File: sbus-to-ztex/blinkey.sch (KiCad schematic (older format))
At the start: 16 parts

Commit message: Commit first go at v1.2
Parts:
- removed D1, D5: RED, LED_SMD:LED_0805_2012Metric, symbol Device:LED_ALT
- removed D2, D6: ORANGE, LED_SMD:LED_0805_2012Metric, symbol Device:LED_ALT
- removed D3, D7: GREEN, LED_SMD:LED_0805_2012Metric, symbol Device:LED_ALT
- removed D4, D8: BLUE, LED_SMD:LED_0805_2012Metric, symbol Device:LED_ALT
- removed R1, R2, R3, R4, R5, R6, R7, R8: 549, Resistor_SMD:R_0603_1608Metric, symbol Device:R
- added J5: Conn_02x06_Odd_Even, Connector_PinSocket_2.54mm:PinSocket_2x06_P2.54mm_Horizontal, symbol Connector_Generic:Conn_02x06_Odd_Even
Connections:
- net GND: now also J5.3 (Pin_3), J5.4 (Pin_4)
- new net +3V3: J5.1 (Pin_1), J5.2 (Pin_2)
- new net PMOD-10: J5.10 (Pin_10)
- new net PMOD-11: J5.11 (Pin_11)
- new net PMOD-12: J5.12 (Pin_12)
- new net PMOD-5: J5.5 (Pin_5)
- new net PMOD-6: J5.6 (Pin_6)
- new net PMOD-7: J5.7 (Pin_7)
- new net PMOD-8: J5.8 (Pin_8)
- new net PMOD-9: J5.9 (Pin_9)

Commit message: fix footprints for SeeedStudio DRC results
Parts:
- J5: footprint Connector_PinSocket_2.54mm:PinSocket_2x06_P2.54mm_Horizontal -> For_SeeedStudio:PinSocket_2x06_P2.54mm_Horizontal_For_SeeedStudio
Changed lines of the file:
@@
 F 0 "J5" H 5650 2167 50  0000 C CNN
 F 1 "Conn_02x06_Odd_Even" H 5650 2076 50  0000 C CNN
-F 2 "Connector_PinSocket_2.54mm:PinSocket_2x06_P2.54mm_Horizontal" H 5600 1750 50  0001 C CNN
+F 2 "For_SeeedStudio:PinSocket_2x06_P2.54mm_Horizontal_For_SeeedStudio" H 5600 1750 50  0001 C CNN
 F 3 "~" H 5600 1750 50  0001 C CNN
 F 4 "A2541HWR-2x6P" H 5600 1750 50  0001 C CNN "MPN"

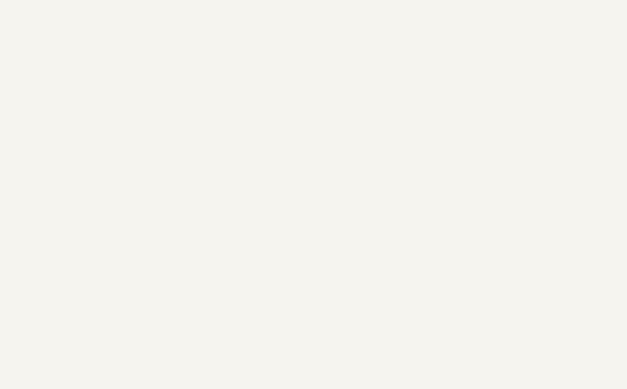
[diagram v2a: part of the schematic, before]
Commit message: update some MPN w/ SeeedStudio replacement
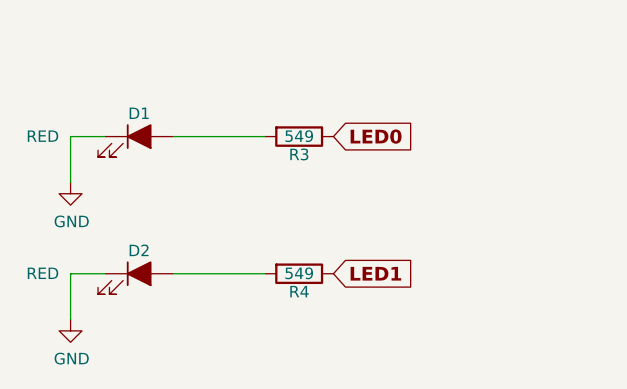
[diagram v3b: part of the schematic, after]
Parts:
- added D1, D2: RED, LED_SMD:LED_0805_2012Metric, symbol Device:LED_ALT
- added R3, R4: 549, Resistor_SMD:R_0603_1608Metric, symbol Device:R
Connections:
- net GND: now also D1.1 (K), D2.1 (K)
- new net: D1.2 (A), R3.2
- new net: D2.2 (A), R4.2
- new net LED0: R3.1
- new net LED1: R4.1
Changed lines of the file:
@@
 Text GLabel 5400 2050 0    50   Input ~ 0
 PMOD-11
+Wire Wire Line
+	2000 1800 1850 1800
+Wire Wire Line
+	1850 1800 1850 2000
+Wire Wire Line
+	2300 1800 2700 1800
+$Comp
+L Device:R R3
+U 1 1 60DF1D6E
+P 2850 1800
+AR Path="/5F6B165A/60DF1D6E" Ref="R3"  Part="1"
+AR Path="/5F67E4B9/60DF1D6E" Ref="R?"  Part="1"
+F 0 "R3" V 2930 1800 50  0000 C CNN
+F 1 "549" V 2850 1800 50  0000 C CNN
+F 2 "Resistor_SMD:R_0603_1608Metric" V 2780 1800 50  0001 C CNN
+F 3 "" H 2850 1800 50  0000 C CNN
+F 4 "0603WAF5490T5E" V 2850 1800 50  0001 C CNN "MPN"
+	1    2850 1800
+	0    1    1    0
+$EndComp
+$Comp
+L Device:LED_ALT D1
+U 1 1 60DF1D7F
+P 2150 1800
+AR Path="/5F6B165A/60DF1D7F" Ref="D1"  Part="1"
+AR Path="/5F67E4B9/60DF1D7F" Ref="D?"  Part="1"
+F 0 "D1" H 2150 1900 50  0000 C CNN
+F 1 "RED" H 1800 1800 50  0000 R CNN
+F 2 "LED_SMD:LED_0805_2012Metric" H 2150 1800 50  0001 C CNN
+F 3 "https://optoelectronics.liteon.com/upload/download/DS-22-99-0150/LTST-C170KRKT.pdf" H 2150 1800 50  0001 C CNN
+F 4 "www.liteon.com" H 2150 1800 60  0001 C CNN "MNF1_URL"
+F 5 "LTST-C170KRKT" H 2150 1800 60  0001 C CNN "MPN"
+F 6 "859-LTST-C170KRKT" H 2150 1800 60  0001 C CNN "Mouser"
+F 7 "743-IN-S85ATR" H 2150 1800 50  0001 C CNN "Mouse_r2"
+F 8 "160-1415-1-ND" H 2150 1800 50  0001 C CNN "Digikey"
+F 9 "C94868" H 2150 1800 50  0001 C CNN "LCSC"
+F 10 "0.0195$" H 2150 1800 50  0001 C CNN "price400_LCSC"
+F 11 "FV007" H 2150 1800 50  0001 C CNN "Koncar"
+F 12 "TB" H 2150 1800 50  0001 C CNN "Side"
+	1    2150 1800
+	1    0    0    -1
+$EndComp
+$Comp
+L power:GND #PWR0134
+U 1 1 60DF1D86
+P 1850 2000
+F 0 "#PWR0134" H 1850 1750 50  0001 C CNN
+F 1 "GND" H 1855 1827 50  0000 C CNN
+F 2 "" H 1850 2000 50  0001 C CNN
+F 3 "" H 1850 2000 50  0001 C CNN
+	1    1850 2000
+	1    0    0    -1
+$EndComp
+Text GLabel 3000 1800 2    60   Input ~ 12
+LED0
+Wire Wire Line
+	2000 2400 1850 2400
+Wire Wire Line
+	1850 2400 1850 2600
+Wire Wire Line
+	2300 2400 2700 2400
+$Comp
+L Device:R R4
+U 1 1 60DF1E35
+P 2850 2400
+AR Path="/5F6B165A/60DF1E35" Ref="R4"  Part="1"
+AR Path="/5F67E4B9/60DF1E35" Ref="R?"  Part="1"
+F 0 "R4" V 2930 2400 50  0000 C CNN
+F 1 "549" V 2850 2400 50  0000 C CNN
+F 2 "Resistor_SMD:R_0603_1608Metric" V 2780 2400 50  0001 C CNN
+F 3 "" H 2850 2400 50  0000 C CNN
+F 4 "0603WAF5490T5E" V 2850 2400 50  0001 C CNN "MPN"
+	1    2850 2400
+	0    1    1    0
+$EndComp
+$Comp
+L Device:LED_ALT D2
+U 1 1 60DF1E46
+P 2150 2400
+AR Path="/5F6B165A/60DF1E46" Ref="D2"  Part="1"
+AR Path="/5F67E4B9/60DF1E46" Ref="D?"  Part="1"
+F 0 "D2" H 2150 2500 50  0000 C CNN
+F 1 "RED" H 1800 2400 50  0000 R CNN
+F 2 "LED_SMD:LED_0805_2012Metric" H 2150 2400 50  0001 C CNN
+F 3 "https://optoelectronics.liteon.com/upload/download/DS-22-99-0150/LTST-C170KRKT.pdf" H 2150 2400 50  0001 C CNN
+F 4 "www.liteon.com" H 2150 2400 60  0001 C CNN "MNF1_URL"
+F 5 "LTST-C170KRKT" H 2150 2400 60  0001 C CNN "MPN"
+F 6 "859-LTST-C170KRKT" H 2150 2400 60  0001 C CNN "Mouser"
+F 7 "743-IN-S85ATR" H 2150 2400 50  0001 C CNN "Mouse_r2"
+F 8 "160-1415-1-ND" H 2150 2400 50  0001 C CNN "Digikey"
+F 9 "C94868" H 2150 2400 50  0001 C CNN "LCSC"
+F 10 "0.0195$" H 2150 2400 50  0001 C CNN "price400_LCSC"
+F 11 "FV007" H 2150 2400 50  0001 C CNN "Koncar"
+F 12 "TB" H 2150 2400 50  0001 C CNN "Side"
+	1    2150 2400
+	1    0    0    -1
+$EndComp
+$Comp
+L power:GND #PWR0135
+U 1 1 60DF1E4D
+P 1850 2600
+F 0 "#PWR0135" H 1850 2350 50  0001 C CNN
+F 1 "GND" H 1855 2427 50  0000 C CNN
+F 2 "" H 1850 2600 50  0001 C CNN
+F 3 "" H 1850 2600 50  0001 C CNN
+	1    1850 2600
+	1    0    0    -1
+$EndComp
+Text GLabel 3000 2400 2    60   Input ~ 12
+LED1
 $EndSCHEMATC

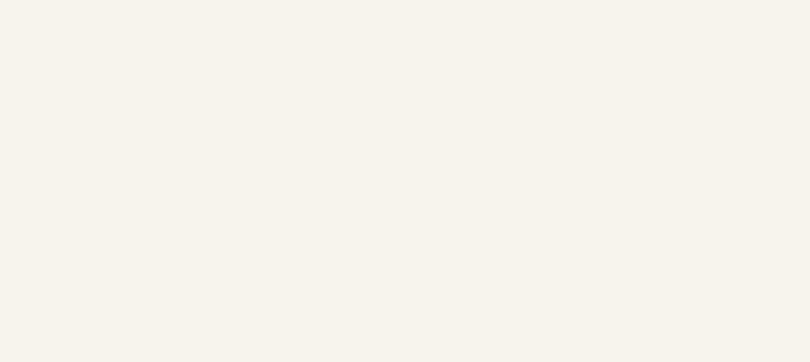
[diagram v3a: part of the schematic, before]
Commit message: add a pwr header (for e.g. non-pwm fan)
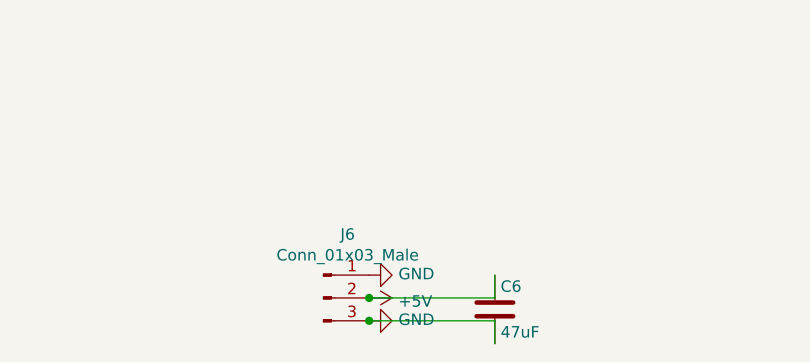
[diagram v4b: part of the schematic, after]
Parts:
- added C6: 47uF, Capacitor_SMD:C_0805_2012Metric, symbol Device:C
- added J6: Conn_01x03_Male, Connector_Molex:Molex_KK-254_AE-6410-03A_1x03_P2.54mm_Vertical, symbol Connector:Conn_01x03_Male
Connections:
- net GND: now also C6.2, J6.1 (Pin_1), J6.3 (Pin_3)
- new net +5V: C6.1, J6.2 (Pin_2)
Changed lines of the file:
@@
 Text GLabel 3000 2400 2    60   Input ~ 12
 LED1
+$Comp
+L Connector:Conn_01x03_Male J6
+U 1 1 60E1E49E
+P 4400 4750
+F 0 "J6" H 4506 5028 50  0000 C CNN
+F 1 "Conn_01x03_Male" H 4506 4937 50  0000 C CNN
+F 2 "Connector_Molex:Molex_KK-254_AE-6410-03A_1x03_P2.54mm_Vertical" H 4400 4750 50  0001 C CNN
+F 3 "~" H 4400 4750 50  0001 C CNN
+	1    4400 4750
+	1    0    0    -1
+$EndComp
+$Comp
+L power:GND #PWR0136
+U 1 1 60E1EC2C
+P 4600 4650
+F 0 "#PWR0136" H 4600 4400 50  0001 C CNN
+F 1 "GND" V 4605 4522 50  0000 R CNN
+F 2 "" H 4600 4650 50  0001 C CNN
+F 3 "" H 4600 4650 50  0001 C CNN
+	1    4600 4650
+	0    -1   -1   0
+$EndComp
+$Comp
+L power:+5V #PWR0137
+U 1 1 60E1ED6C
+P 4600 4750
+F 0 "#PWR0137" H 4600 4600 50  0001 C CNN
+F 1 "+5V" V 4615 4878 50  0000 L CNN
+F 2 "" H 4600 4750 50  0001 C CNN
+F 3 "" H 4600 4750 50  0001 C CNN
+	1    4600 4750
+	0    1    1    0
+$EndComp
+$Comp
+L power:GND #PWR0138
+U 1 1 60E1FA97
+P 4600 4850
+F 0 "#PWR0138" H 4600 4600 50  0001 C CNN
+F 1 "GND" V 4605 4722 50  0000 R CNN
+F 2 "" H 4600 4850 50  0001 C CNN
+F 3 "" H 4600 4850 50  0001 C CNN
+	1    4600 4850
+	0    -1   -1   0
+$EndComp
+$Comp
+L Device:C C?
+U 1 1 60E24715
+P 5150 4800
+AR Path="/5F69F4EF/60E24715" Ref="C?"  Part="1"
+AR Path="/5F6B165A/60E24715" Ref="C6"  Part="1"
+F 0 "C6" H 5175 4900 50  0000 L CNN
+F 1 "47uF" H 5175 4700 50  0000 L CNN
+F 2 "Capacitor_SMD:C_0805_2012Metric" H 5188 4650 50  0001 C CNN
+F 3 "" H 5150 4800 50  0000 C CNN
+F 4 "GRM21BR60J476ME15L" H 5150 4800 50  0001 C CNN "MPN"
+	1    5150 4800
+	1    0    0    -1
+$EndComp
+Wire Wire Line
+	4600 4750 5150 4750
+Wire Wire Line
+	5150 4750 5150 4650
+Connection ~ 4600 4750
+Wire Wire Line
+	4600 4850 5150 4850
+Wire Wire Line
+	5150 4850 5150 4950
+Connection ~ 4600 4850
 $EndSCHEMATC

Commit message: more up-to-date
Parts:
- J6: MPN (none) -> 640456-3; MPN-ALT (none) -> 22-27-2031; Manufacturer (none) -> TE Connectivity; Manufacturer-ALT (none) -> Molex; URL-ALT (none) -> https://www.mouser.fr/ProductDetail/Molex/22-27-2031?qs=%2F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
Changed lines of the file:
@@
 F 2 "Connector_Molex:Molex_KK-254_AE-6410-03A_1x03_P2.54mm_Vertical" H 4400 4750 50  0001 C CNN
 F 3 "~" H 4400 4750 50  0001 C CNN
+F 4 "22-27-2031" H 4400 4750 50  0001 C CNN "MPN-ALT"
+F 5 "Molex" H 4400 4750 50  0001 C CNN "Manufacturer-ALT"
+F 6 "https://www.mouser.fr/ProductDetail/Molex/22-27-2031?qs=%2Fha2pyFadugXOaGYK9vaczm7nZ04txhJn3OGcnGWT3U=" H 4400 4750 50  0001 C CNN "URL-ALT"
+F 7 "640456-3" H 4400 4750 50  0001 C CNN "MPN"
+F 8 "TE Connectivity" H 4400 4750 50  0001 C CNN "Manufacturer"
 	1    4400 4750
 	1    0    0    -1

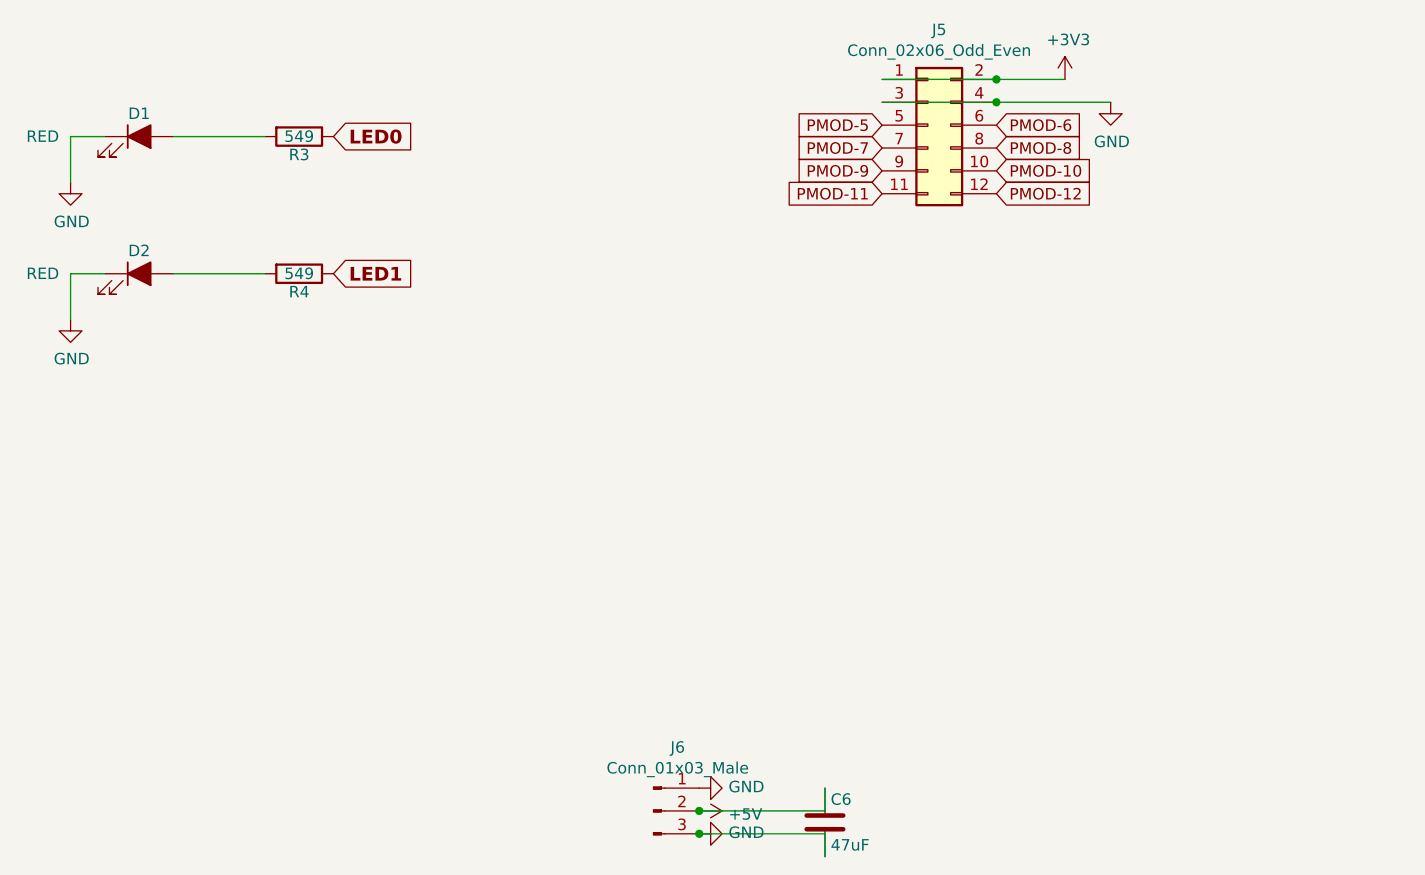
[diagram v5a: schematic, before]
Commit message: Fewer LEDs, more interrupts, replace USB VBus power chip by something that might be available..., update signals file
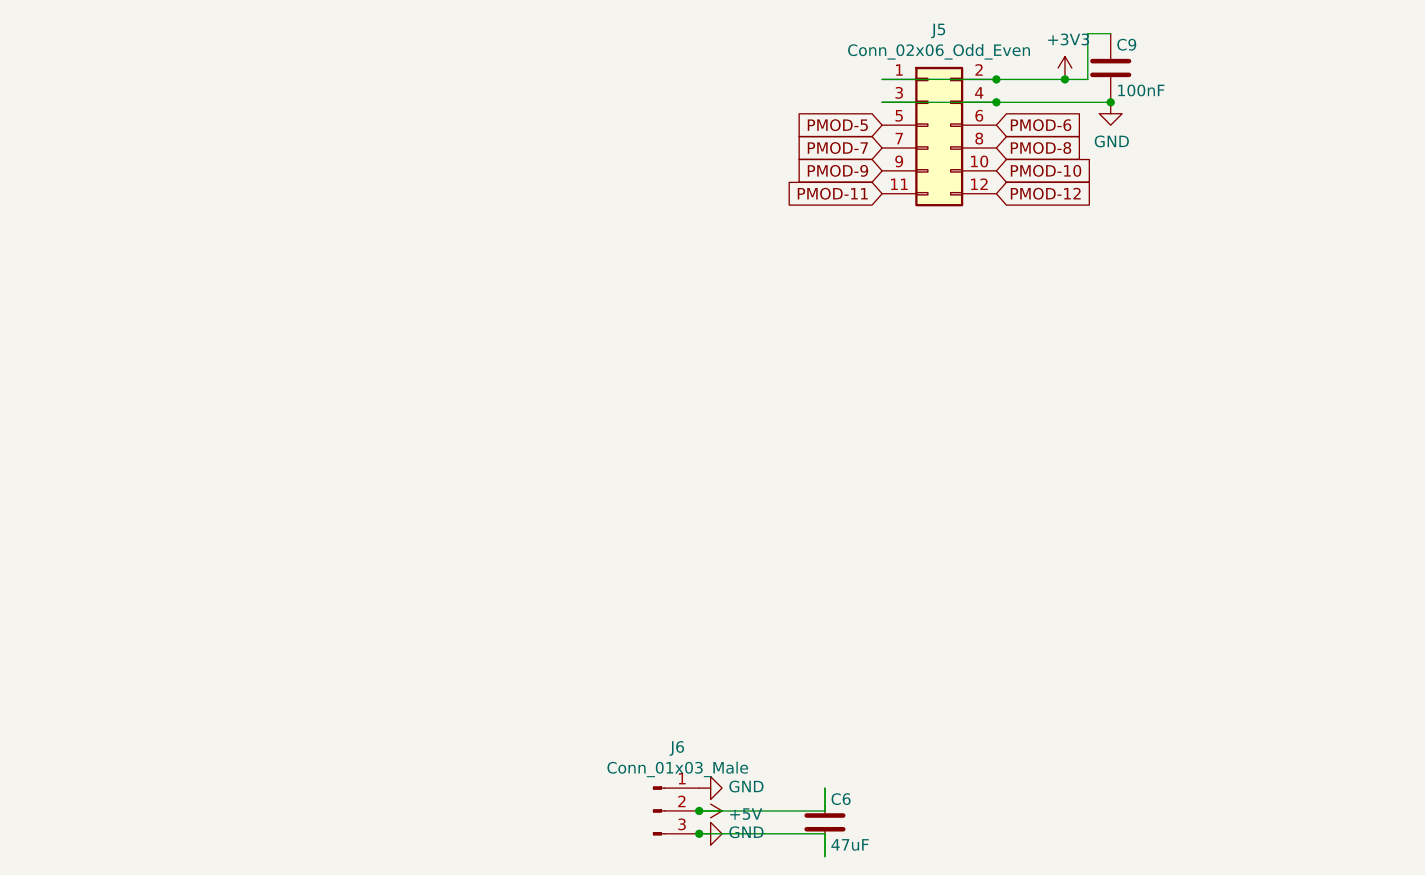
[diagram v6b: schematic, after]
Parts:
- removed D1, D2: RED, LED_SMD:LED_0805_2012Metric, symbol Device:LED_ALT
- removed R3, R4: 549, Resistor_SMD:R_0603_1608Metric, symbol Device:R
- added C9: 100nF, Capacitor_SMD:C_0603_1608Metric, symbol Device:C
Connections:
- net +3V3: now also C9.1
- net GND: now also C9.2
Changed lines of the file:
@@
 Text GLabel 5400 2050 0    50   Input ~ 0
 PMOD-11
-Wire Wire Line
-	2000 1800 1850 1800
-Wire Wire Line
-	1850 1800 1850 2000
-Wire Wire Line
-	2300 1800 2700 1800
-$Comp
-L Device:R R3
-U 1 1 60DF1D6E
-P 2850 1800
-AR Path="/5F6B165A/60DF1D6E" Ref="R3"  Part="1"
-AR Path="/5F67E4B9/60DF1D6E" Ref="R?"  Part="1"
-F 0 "R3" V 2930 1800 50  0000 C CNN
-F 1 "549" V 2850 1800 50  0000 C CNN
-F 2 "Resistor_SMD:R_0603_1608Metric" V 2780 1800 50  0001 C CNN
-F 3 "" H 2850 1800 50  0000 C CNN
-F 4 "0603WAF5490T5E" V 2850 1800 50  0001 C CNN "MPN"
-	1    2850 1800
-	0    1    1    0
-$EndComp
-$Comp
-L Device:LED_ALT D1
-U 1 1 60DF1D7F
-P 2150 1800
-AR Path="/5F6B165A/60DF1D7F" Ref="D1"  Part="1"
-AR Path="/5F67E4B9/60DF1D7F" Ref="D?"  Part="1"
-F 0 "D1" H 2150 1900 50  0000 C CNN
-F 1 "RED" H 1800 1800 50  0000 R CNN
-F 2 "LED_SMD:LED_0805_2012Metric" H 2150 1800 50  0001 C CNN
-F 3 "https://optoelectronics.liteon.com/upload/download/DS-22-99-0150/LTST-C170KRKT.pdf" H 2150 1800 50  0001 C CNN
-F 4 "www.liteon.com" H 2150 1800 60  0001 C CNN "MNF1_URL"
-F 5 "LTST-C170KRKT" H 2150 1800 60  0001 C CNN "MPN"
-F 6 "859-LTST-C170KRKT" H 2150 1800 60  0001 C CNN "Mouser"
-F 7 "743-IN-S85ATR" H 2150 1800 50  0001 C CNN "Mouse_r2"
-F 8 "160-1415-1-ND" H 2150 1800 50  0001 C CNN "Digikey"
-F 9 "C94868" H 2150 1800 50  0001 C CNN "LCSC"
-F 10 "0.0195$" H 2150 1800 50  0001 C CNN "price400_LCSC"
-F 11 "FV007" H 2150 1800 50  0001 C CNN "Koncar"
-F 12 "TB" H 2150 1800 50  0001 C CNN "Side"
-	1    2150 1800
-	1    0    0    -1
-$EndComp
-$Comp
-L power:GND #PWR0134
-U 1 1 60DF1D86
-P 1850 2000
-F 0 "#PWR0134" H 1850 1750 50  0001 C CNN
-F 1 "GND" H 1855 1827 50  0000 C CNN
-F 2 "" H 1850 2000 50  0001 C CNN
-F 3 "" H 1850 2000 50  0001 C CNN
-	1    1850 2000
-	1    0    0    -1
-$EndComp
-Text GLabel 3000 1800 2    60   Input ~ 12
-LED0
-Wire Wire Line
-	2000 2400 1850 2400
-Wire Wire Line
-	1850 2400 1850 2600
-Wire Wire Line
-	2300 2400 2700 2400
-$Comp
-L Device:R R4
-U 1 1 60DF1E35
-P 2850 2400
-AR Path="/5F6B165A/60DF1E35" Ref="R4"  Part="1"
-AR Path="/5F67E4B9/60DF1E35" Ref="R?"  Part="1"
-F 0 "R4" V 2930 2400 50  0000 C CNN
-F 1 "549" V 2850 2400 50  0000 C CNN
-F 2 "Resistor_SMD:R_0603_1608Metric" V 2780 2400 50  0001 C CNN
-F 3 "" H 2850 2400 50  0000 C CNN
-F 4 "0603WAF5490T5E" V 2850 2400 50  0001 C CNN "MPN"
-	1    2850 2400
-	0    1    1    0
-$EndComp
-$Comp
-L Device:LED_ALT D2
-U 1 1 60DF1E46
-P 2150 2400
-AR Path="/5F6B165A/60DF1E46" Ref="D2"  Part="1"
-AR Path="/5F67E4B9/60DF1E46" Ref="D?"  Part="1"
-F 0 "D2" H 2150 2500 50  0000 C CNN
-F 1 "RED" H 1800 2400 50  0000 R CNN
-F 2 "LED_SMD:LED_0805_2012Metric" H 2150 2400 50  0001 C CNN
-F 3 "https://optoelectronics.liteon.com/upload/download/DS-22-99-0150/LTST-C170KRKT.pdf" H 2150 2400 50  0001 C CNN
-F 4 "www.liteon.com" H 2150 2400 60  0001 C CNN "MNF1_URL"
-F 5 "LTST-C170KRKT" H 2150 2400 60  0001 C CNN "MPN"
-F 6 "859-LTST-C170KRKT" H 2150 2400 60  0001 C CNN "Mouser"
-F 7 "743-IN-S85ATR" H 2150 2400 50  0001 C CNN "Mouse_r2"
-F 8 "160-1415-1-ND" H 2150 2400 50  0001 C CNN "Digikey"
-F 9 "C94868" H 2150 2400 50  0001 C CNN "LCSC"
-F 10 "0.0195$" H 2150 2400 50  0001 C CNN "price400_LCSC"
-F 11 "FV007" H 2150 2400 50  0001 C CNN "Koncar"
-F 12 "TB" H 2150 2400 50  0001 C CNN "Side"
-	1    2150 2400
-	1    0    0    -1
-$EndComp
-$Comp
-L power:GND #PWR0135
-U 1 1 60DF1E4D
-P 1850 2600
-F 0 "#PWR0135" H 1850 2350 50  0001 C CNN
-F 1 "GND" H 1855 2427 50  0000 C CNN
-F 2 "" H 1850 2600 50  0001 C CNN
-F 3 "" H 1850 2600 50  0001 C CNN
-	1    1850 2600
-	1    0    0    -1
-$EndComp
-Text GLabel 3000 2400 2    60   Input ~ 12
-LED1
 $Comp
 L Connector:Conn_01x03_Male J6
@@
 	5150 4850 5150 4950
 Connection ~ 4600 4850
+$Comp
+L Device:C C?
+U 1 1 612C3C5C
+P 6400 1500
+AR Path="/5F679B53/612C3C5C" Ref="C?"  Part="1"
+AR Path="/5F6B165A/612C3C5C" Ref="C9"  Part="1"
+F 0 "C9" H 6425 1600 50  0000 L CNN
+F 1 "100nF" H 6425 1400 50  0000 L CNN
+F 2 "Capacitor_SMD:C_0603_1608Metric" H 6438 1350 50  0001 C CNN
+F 3 "" H 6400 1500 50  0000 C CNN
+F 4 "www.yageo.com" H 6400 1500 50  0001 C CNN "MNF1_URL"
+F 5 "CC0603KRX7R8BB104" H 6400 1500 50  0001 C CNN "MPN"
+F 6 "603-CC603KRX7R8BB104" H 6400 1500 50  0001 C CNN "Mouser"
+F 7 "?" H 6400 1500 50  0001 C CNN "Digikey"
+F 8 "?" H 6400 1500 50  0001 C CNN "LCSC"
+F 9 "?" H 6400 1500 50  0001 C CNN "Koncar"
+F 10 "TB" H 6400 1500 50  0001 C CNN "Side"
+	1    6400 1500
+	1    0    0    -1
+$EndComp
+Connection ~ 6400 1650
+Wire Wire Line
+	6200 1550 6300 1550
+Wire Wire Line
+	6300 1550 6300 1350
+Wire Wire Line
+	6300 1350 6400 1350
+Connection ~ 6200 1550
 $EndSCHEMATC
